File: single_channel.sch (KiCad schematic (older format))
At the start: 40 parts, among them Q201 BC309B, Q202 BC237B, Q203 BD135, Q204 BD136, Q205 BD243C, Q206 BD244C

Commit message: Finished placement and routing.
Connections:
- net at C207.2, C208.1, Q203.1 (E)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: now also R215.3; no longer R215.1
- net at R217.2, R218.2, R219.1: now also R215.1; no longer R215.3

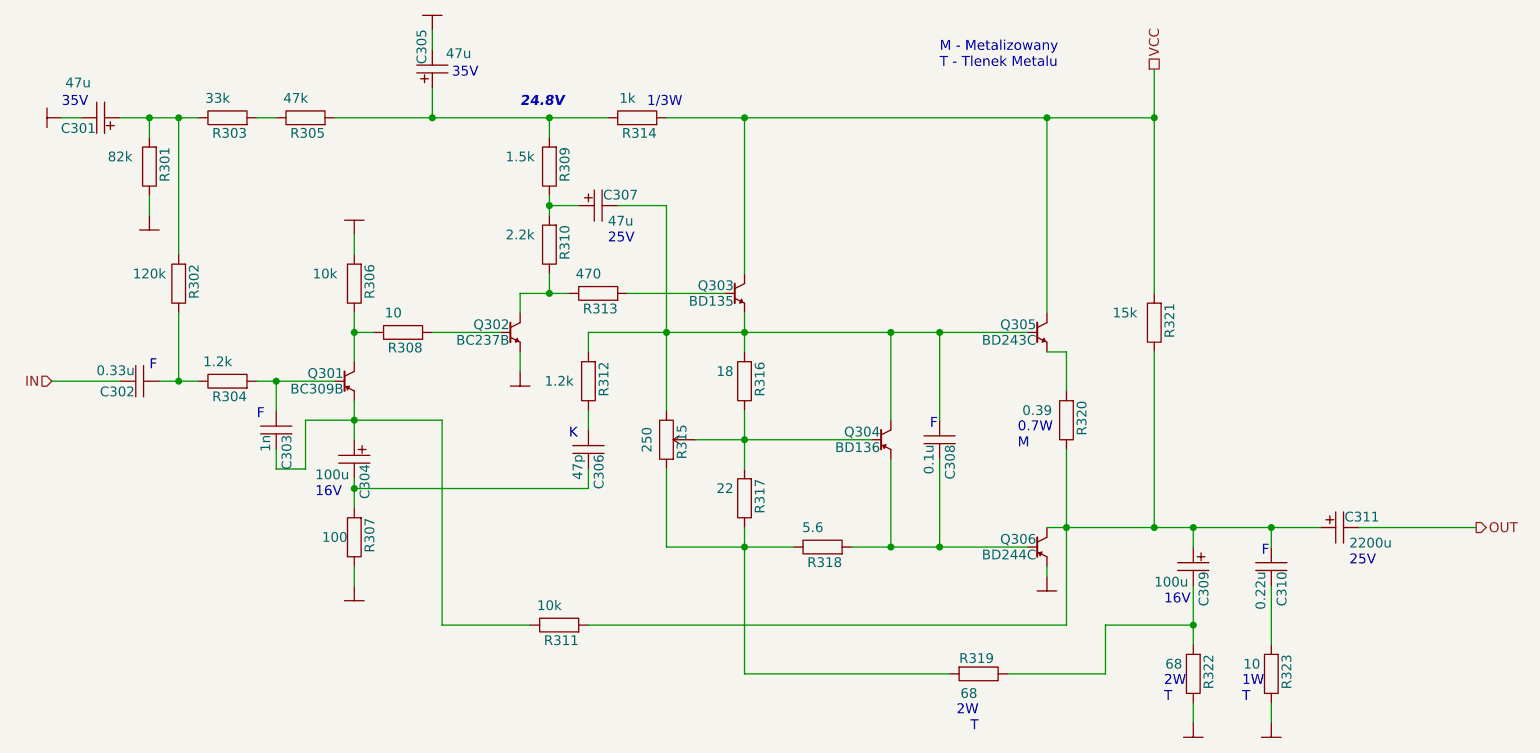
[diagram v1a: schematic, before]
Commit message: Fixed transistors with swapped E-C
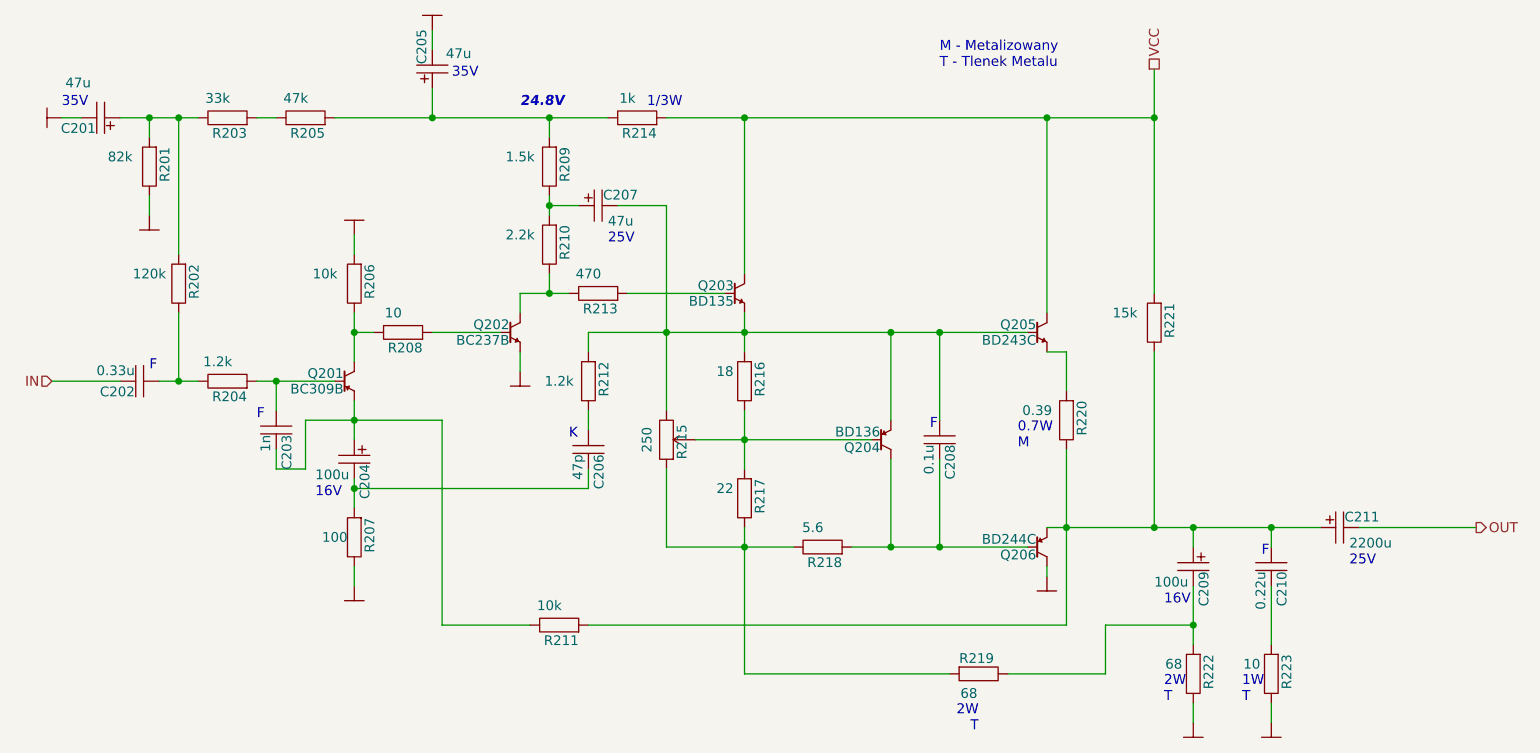
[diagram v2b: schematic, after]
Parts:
- R222: footprint Newlib:RESA_D40L110 -> Newlib:RESR_D40P40
- R223: footprint Newlib:RESA_D30L90 -> Newlib:RESR_D30P40
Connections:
- net GND: now also Q206.2 (C); no longer Q206.3 (E)
- net at C209.1, C210.1, C211.1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: now also Q206.3 (E); no longer Q206.2 (C)
- net at C207.2, C208.1, Q203.1 (E)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: now also Q204.1 (E); no longer Q204.2 (C)
- net at C208.2, Q206.1 (B), R218.1: now also Q204.2 (C); no longer Q204.1 (E)

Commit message: Updated PCB layout to reflect changes in footprints.
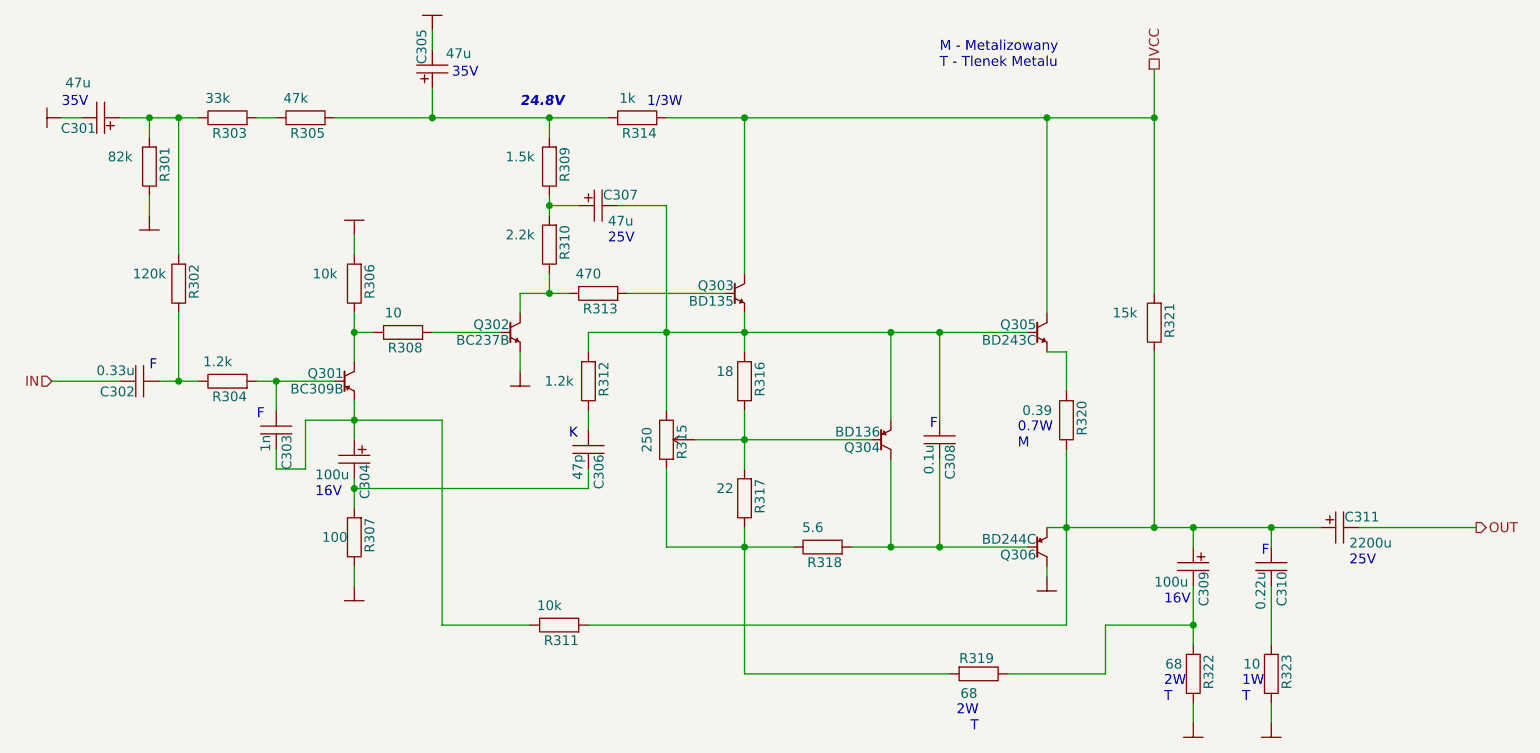
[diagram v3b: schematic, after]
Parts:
- C202: footprint Newlib:CAPRR_P50W45L72 -> Newlib:CAPRR_P50W35L72
- C206: footprint Newlib:C0805 -> Newlib:CAPRR_P30W20L40
- C210: footprint Newlib:CAPRR_P50W50L72 -> Newlib:CAPRR_P50W35L72
- R201, R202, R203, R204, R205, R206, R207, R208, R209, R210, R211, R212, R213, R216, R217, R218, R221: footprint Newlib:C0805 -> Newlib:R0805
- R214: footprint Newlib:RESA_D20L40 -> Newlib:RESR_D40P50
- R215: footprint Newlib:RM-65 -> Newlib:POT-3339P
- R219: footprint Newlib:RESA_D40L110 -> Newlib:RESR_D40P50
